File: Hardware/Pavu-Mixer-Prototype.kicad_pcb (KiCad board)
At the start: 2 copper layers, 155.9 x 91.9 mm, 65 parts, among them J1 Conn_02x16_Counter_Clockwise, U1 74HC595, U2 74HC595, U3 74HC595, U4 PCA9555D, U5 PCA9536D

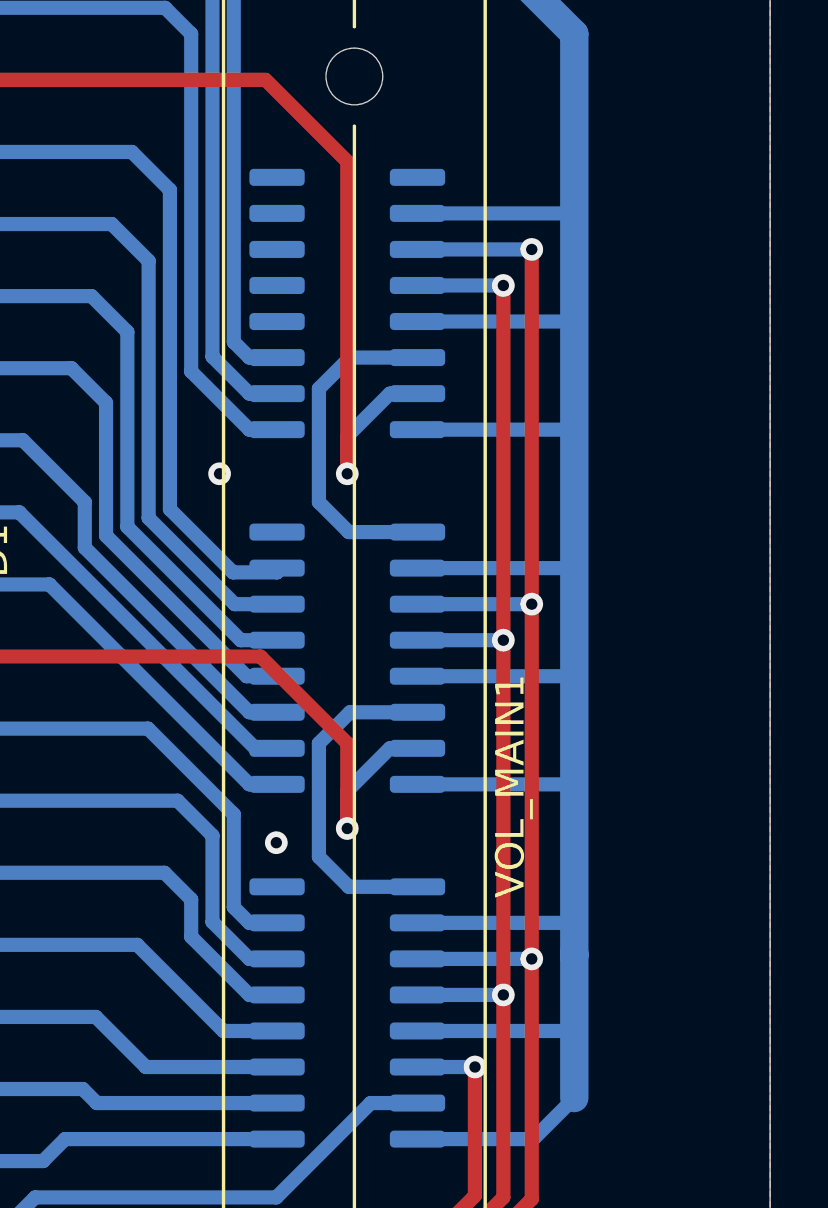
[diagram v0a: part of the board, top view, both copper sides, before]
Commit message: Fix shift register OE being pulled high instead of low
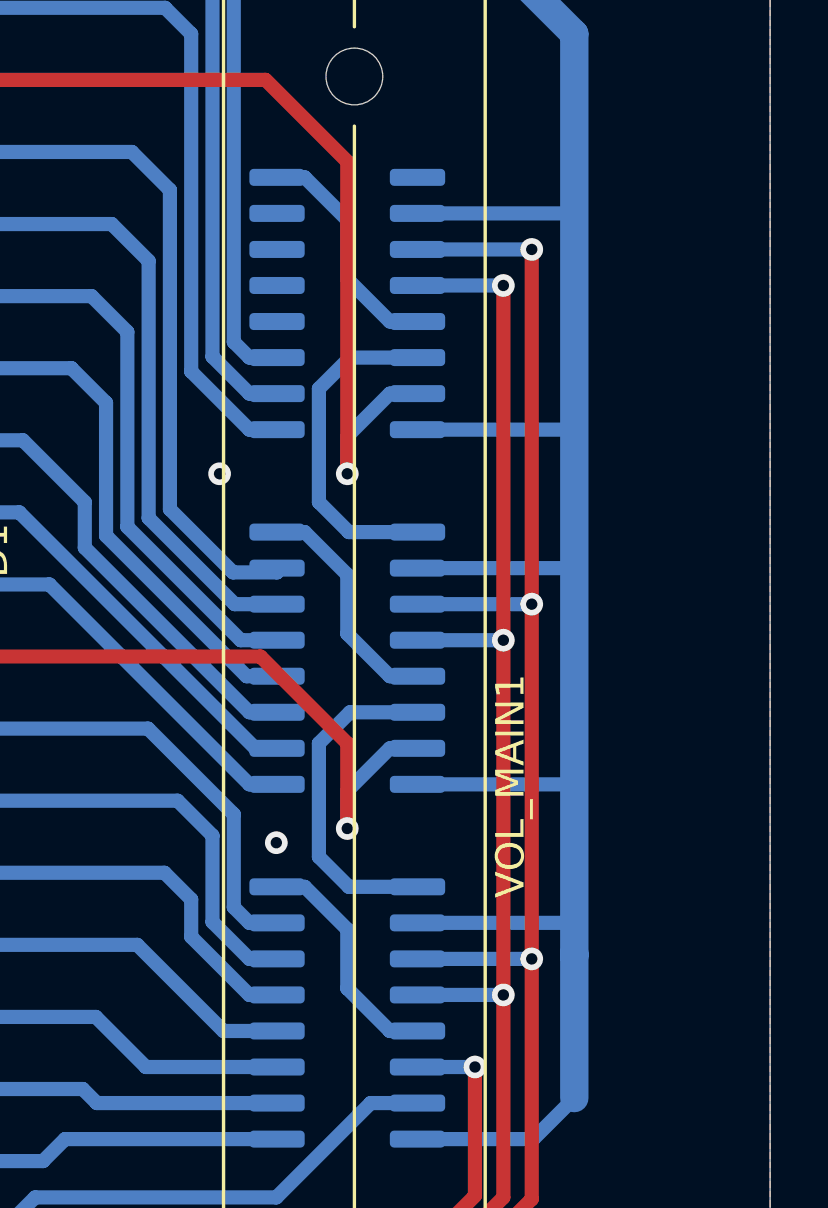
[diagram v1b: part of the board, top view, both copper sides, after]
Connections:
- U1 pad 13: +3V3 -> GND
- U2 pad 13: +3V3 -> GND
- U3 pad 13: +3V3 -> GND
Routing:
- net GND: track 0.00 -> 24.8 mm
- net +3V3: track 473.3 -> 456.7 mm
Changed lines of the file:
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@@
     (thickness 1.6)
     (drawings 6)
-    (tracks 641)
+    (tracks 653)
     (zones 0)
     (modules 65)
@@
       (net 71 MAINVOL_SER))
     (pad 13 smd roundrect (at 2.475 0.635) (size 1.95 0.6) (layers B.Cu B.Paste B.Mask) (roundrect_rratio 0.25)
-      (net 52 +3V3))
+      (net 1 GND))
     (pad 12 smd roundrect (at 2.475 -0.635) (size 1.95 0.6) (layers B.Cu B.Paste B.Mask) (roundrect_rratio 0.25)
       (net 69 MAINVOL_RCLK))
@@
       (net 99 "Net-(U2-Pad14)"))
     (pad 13 smd roundrect (at 2.475 0.635) (size 1.95 0.6) (layers B.Cu B.Paste B.Mask) (roundrect_rratio 0.25)
-      (net 52 +3V3))
+      (net 1 GND))
     (pad 12 smd roundrect (at 2.475 -0.635) (size 1.95 0.6) (layers B.Cu B.Paste B.Mask) (roundrect_rratio 0.25)
       (net 69 MAINVOL_RCLK))
@@
       (net 98 "Net-(U1-Pad14)"))
     (pad 13 smd roundrect (at 2.475 0.635) (size 1.95 0.6) (layers B.Cu B.Paste B.Mask) (roundrect_rratio 0.25)
-      (net 52 +3V3))
+      (net 1 GND))
     (pad 12 smd roundrect (at 2.475 -0.635) (size 1.95 0.6) (layers B.Cu B.Paste B.Mask) (roundrect_rratio 0.25)
       (net 69 MAINVOL_RCLK))
@@
   (via (at 107.95 80.95) (size 0.8) (drill 0.4) (layers F.Cu B.Cu) (net 1))
   (via (at 77.95 70.95) (size 0.8) (drill 0.4) (layers F.Cu B.Cu) (net 1))
+  (segment (start 209.5 108.555) (end 211 110.055) (width 0.5) (layer B.Cu) (net 1))
+  (segment (start 208.525 108.555) (end 209.5 108.555) (width 0.5) (layer B.Cu) (net 1))
+  (segment (start 211 112.135) (end 211 110.055) (width 0.5) (layer B.Cu) (net 1))
+  (segment (start 212.5 113.635) (end 211 112.135) (width 0.5) (layer B.Cu) (net 1))
+  (segment (start 213.475 113.635) (end 212.5 113.635) (width 0.5) (layer B.Cu) (net 1))
+  (segment (start 211 99.635) (end 211 97.555) (width 0.5) (layer B.Cu) (net 1))
+  (segment (start 208.525 96.055) (end 209.5 96.055) (width 0.5) (layer B.Cu) (net 1))
+  (segment (start 209.5 96.055) (end 211 97.555) (width 0.5) (layer B.Cu) (net 1))
+  (segment (start 212.5 101.135) (end 211 99.635) (width 0.5) (layer B.Cu) (net 1))
+  (segment (start 213.475 101.135) (end 212.5 101.135) (width 0.5) (layer B.Cu) (net 1))
+  (segment (start 208.525 83.555) (end 209.5 83.555) (width 0.5) (layer B.Cu) (net 1))
+  (segment (start 211 87.135) (end 211 85.055) (width 0.5) (layer B.Cu) (net 1))
+  (segment (start 209.5 83.555) (end 211 85.055) (width 0.5) (layer B.Cu) (net 1))
+  (segment (start 212.5 88.635) (end 211 87.135) (width 0.5) (layer B.Cu) (net 1))
+  (segment (start 213.475 88.635) (end 212.5 88.635) (width 0.5) (layer B.Cu) (net 1))
   (segment (start 219 111) (end 219 116) (width 1) (layer B.Cu) (net 52))
   (segment (start 219 111) (end 219 110.892998) (width 1) (layer B.Cu) (net 52))
@@
   (segment (start 207.5 70) (end 207.5 72.5) (width 1) (layer B.Cu) (net 52))
   (segment (start 213.475 97.325) (end 219 97.325) (width 0.5) (layer B.Cu) (net 52))
-  (segment (start 213.475 101.135) (end 219 101.135) (width 0.5) (layer B.Cu) (net 52))
   (segment (start 213.475 104.945) (end 219 104.945) (width 0.5) (layer B.Cu) (net 52))
   (segment (start 213.475 109.825) (end 219 109.825) (width 0.5) (layer B.Cu) (net 52))
-  (segment (start 213.475 113.635) (end 219 113.635) (width 0.5) (layer B.Cu) (net 52))
   (segment (start 217.555 117.445) (end 219 116) (width 0.5) (layer B.Cu) (net 52))
   (segment (start 213.475 117.445) (end 217.555 117.445) (width 0.5) (layer B.Cu) (net 52))
   (segment (start 213.475 84.825) (end 219 84.825) (width 0.5) (layer B.Cu) (net 52))
-  (segment (start 213.475 88.635) (end 219 88.635) (width 0.5) (layer B.Cu) (net 52))
   (segment (start 213.475 92.445) (end 219 92.445) (width 0.5) (layer B.Cu) (net 52))
   (segment (start 138.89 62.5) (end 138.89 66.5) (width 1) (layer F.Cu) (net 52))

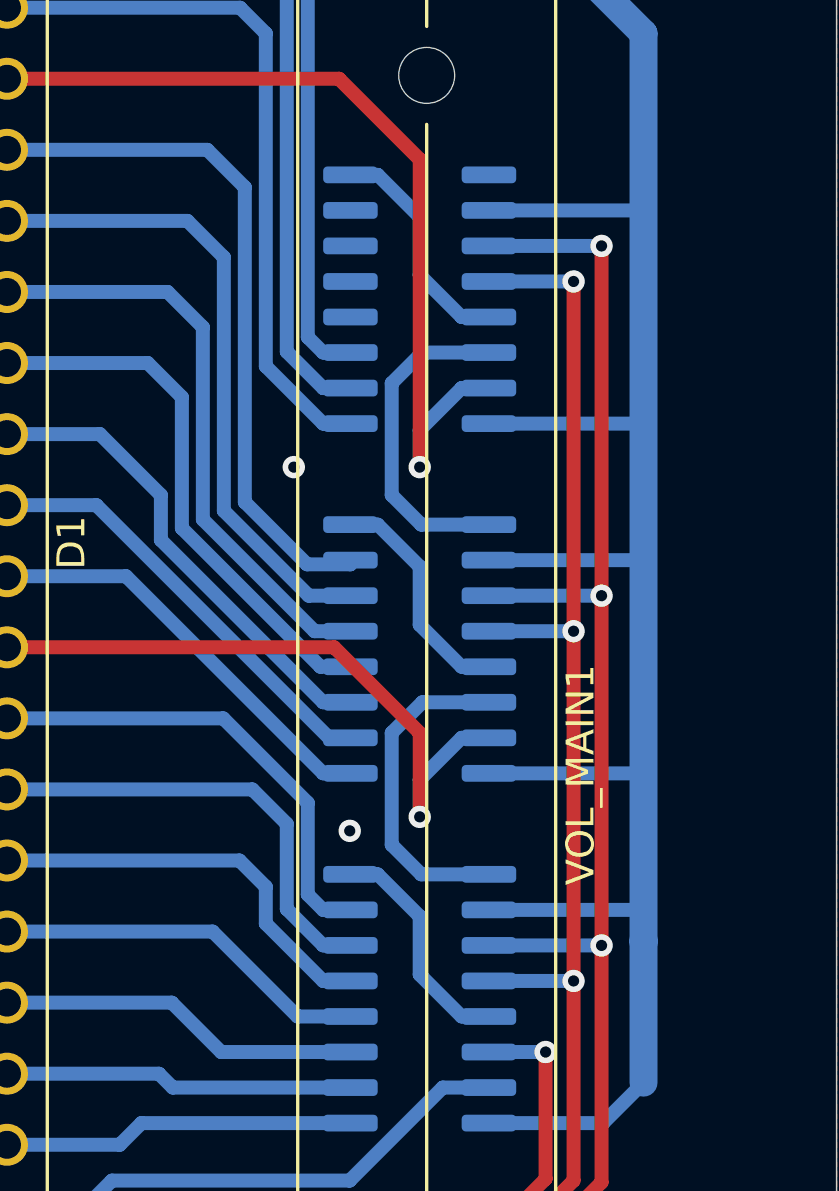
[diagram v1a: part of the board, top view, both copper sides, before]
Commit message: Fix shift register GND connections
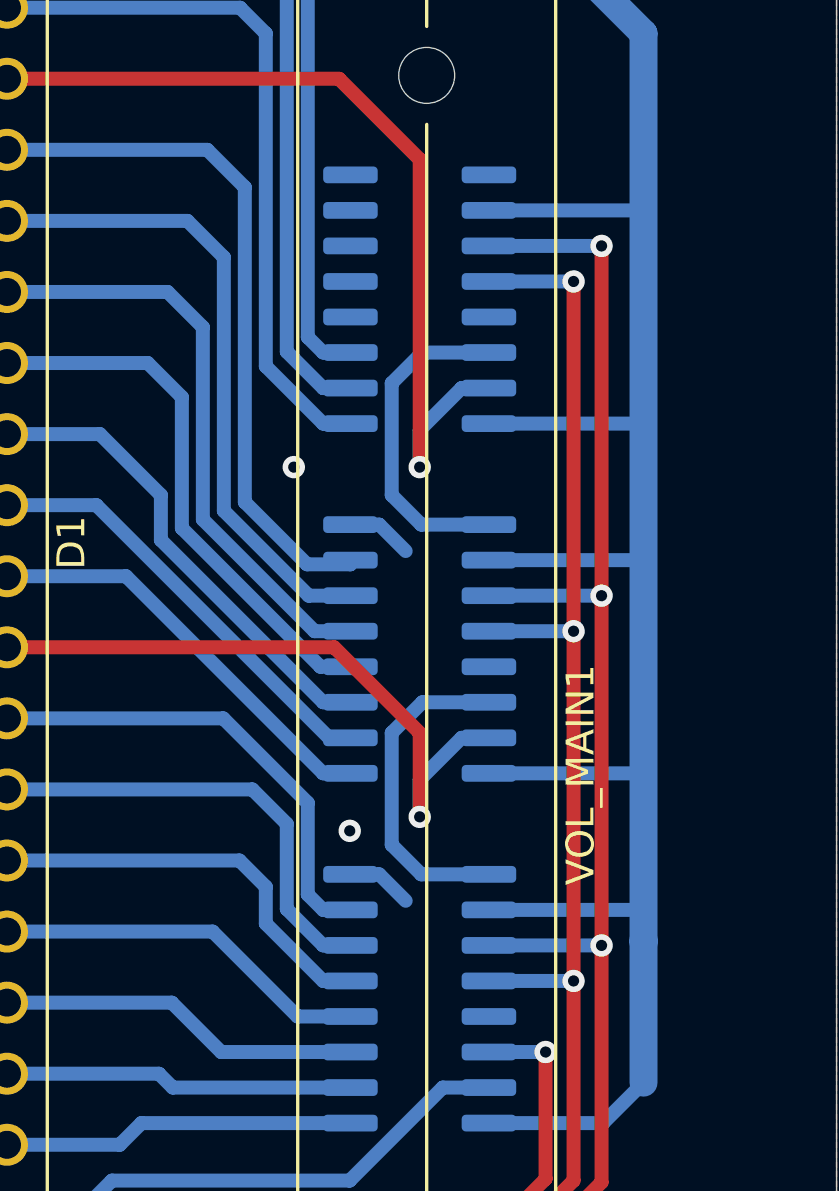
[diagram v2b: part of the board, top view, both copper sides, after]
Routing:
- net GND: track 24.8 -> 4.73 mm
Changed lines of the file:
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@@
     (thickness 1.6)
     (drawings 6)
-    (tracks 653)
+    (tracks 642)
     (zones 0)
     (modules 65)
@@
   (via (at 107.95 80.95) (size 0.8) (drill 0.4) (layers F.Cu B.Cu) (net 1))
   (via (at 77.95 70.95) (size 0.8) (drill 0.4) (layers F.Cu B.Cu) (net 1))
-  (segment (start 209.5 108.555) (end 211 110.055) (width 0.5) (layer B.Cu) (net 1))
-  (segment (start 208.525 108.555) (end 209.5 108.555) (width 0.5) (layer B.Cu) (net 1))
-  (segment (start 211 112.135) (end 211 110.055) (width 0.5) (layer B.Cu) (net 1))
-  (segment (start 212.5 113.635) (end 211 112.135) (width 0.5) (layer B.Cu) (net 1))
-  (segment (start 213.475 113.635) (end 212.5 113.635) (width 0.5) (layer B.Cu) (net 1))
-  (segment (start 211 99.635) (end 211 97.555) (width 0.5) (layer B.Cu) (net 1))
-  (segment (start 208.525 96.055) (end 209.5 96.055) (width 0.5) (layer B.Cu) (net 1))
-  (segment (start 209.5 96.055) (end 211 97.555) (width 0.5) (layer B.Cu) (net 1))
-  (segment (start 212.5 101.135) (end 211 99.635) (width 0.5) (layer B.Cu) (net 1))
-  (segment (start 213.475 101.135) (end 212.5 101.135) (width 0.5) (layer B.Cu) (net 1))
-  (segment (start 208.525 83.555) (end 209.5 83.555) (width 0.5) (layer B.Cu) (net 1))
-  (segment (start 211 87.135) (end 211 85.055) (width 0.5) (layer B.Cu) (net 1))
-  (segment (start 209.5 83.555) (end 211 85.055) (width 0.5) (layer B.Cu) (net 1))
-  (segment (start 212.5 88.635) (end 211 87.135) (width 0.5) (layer B.Cu) (net 1))
-  (segment (start 213.475 88.635) (end 212.5 88.635) (width 0.5) (layer B.Cu) (net 1))
+  (segment (start 208.525 96.055) (end 209.555 96.055) (width 0.5) (layer B.Cu) (net 1))
+  (segment (start 209.555 96.055) (end 210.5 97) (width 0.5) (layer B.Cu) (net 1))
+  (segment (start 209.555 108.555) (end 210.5 109.5) (width 0.5) (layer B.Cu) (net 1))
+  (segment (start 208.525 108.555) (end 209.555 108.555) (width 0.5) (layer B.Cu) (net 1))
   (segment (start 219 111) (end 219 116) (width 1) (layer B.Cu) (net 52))
   (segment (start 219 111) (end 219 110.892998) (width 1) (layer B.Cu) (net 52))
